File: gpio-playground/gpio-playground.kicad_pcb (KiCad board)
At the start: 2 copper layers, 42.2 x 48.7 mm, 47 parts, among them J1 Conn_02x03_Odd_Even, J2 Conn_02x08_Odd_Even, SW0 SW_Push, SW1 SW_Push, SW2 SW_Push, SW3 SW_Push, SW4 SW_Push, SW5 SW_Push, SW6 SW_Push, SW7 SW_Push, U1 BIWIN_DTS04GE_SMD, U2 BIWIN_DTS04GE_SMD, U3 74AHC244

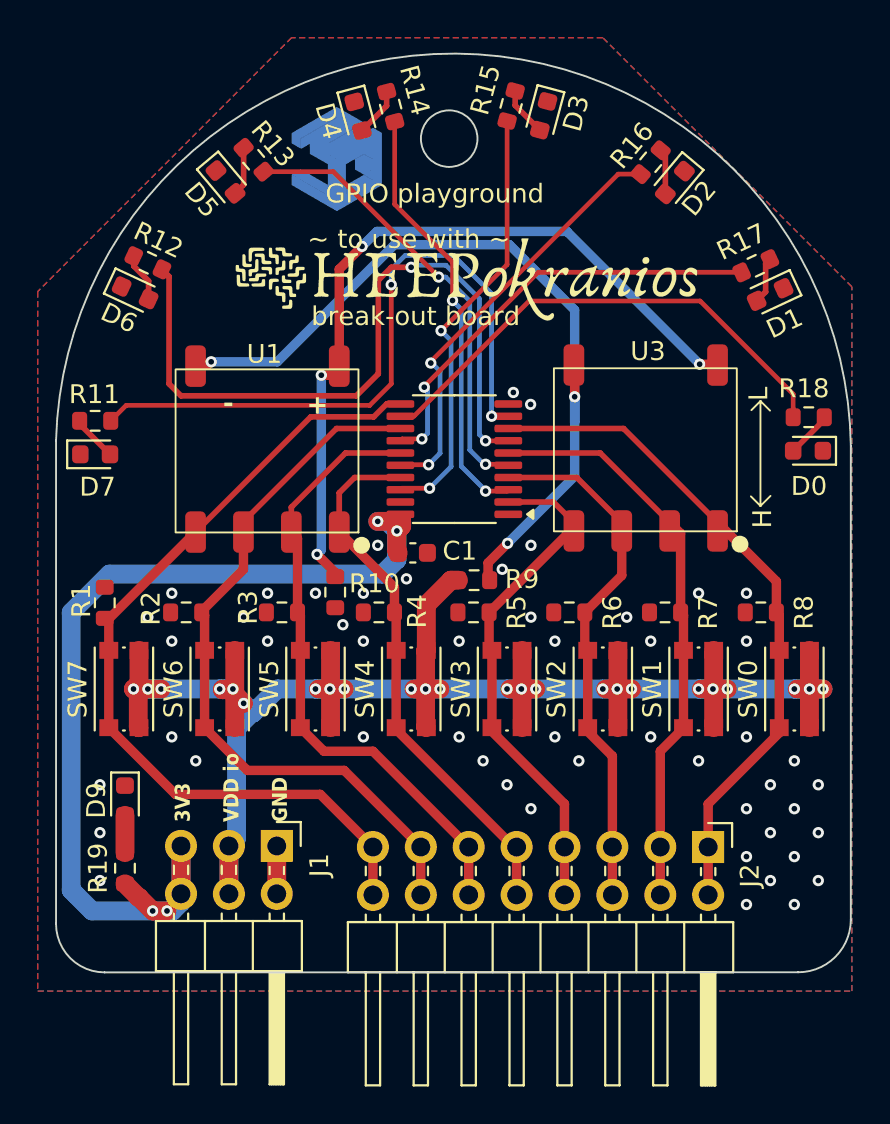
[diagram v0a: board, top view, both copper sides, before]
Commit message: GPIO playground board: Fixed DRCs and shorts in dMUX pin header connections, and re-generated production files (CPL and gerbers)
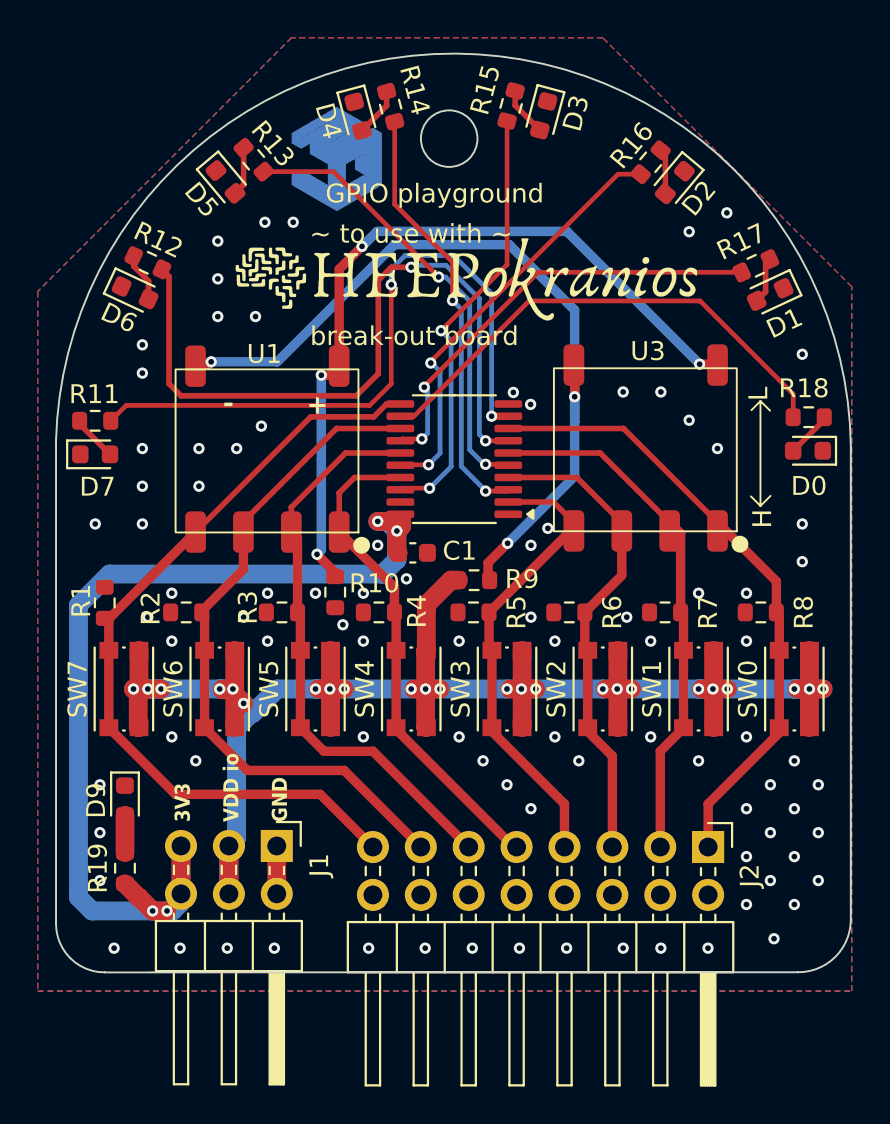
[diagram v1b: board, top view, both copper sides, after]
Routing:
- net /DMUX_7: track 45.2 -> 42.6 mm
- net /DMUX_6: track 38.7 -> 36.1 mm
- net /DMUX_5: track 32.7 -> 30.2 mm
- net /DMUX_4: track 28.6 -> 26.1 mm
- net /DMUX_3: track 27.5 -> 24.9 mm
- net /DMUX_2: track 28.4 -> 25.9 mm
- net /DMUX_1: track 30.9 -> 28.4 mm
- net /DMUX_0: track 36.1 -> 33.5 mm
- net GND: vias 52 -> 90
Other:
- board text added: "GPIO playground v1.0 August 2026"
- board text removed: "GPIO playground v1.0 July 2026"
